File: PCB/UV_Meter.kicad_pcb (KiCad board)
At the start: 2 copper layers, 50.8 x 15.2 mm, 11 parts, among them SW1 SW_Push, U1 ATtiny85-20PU

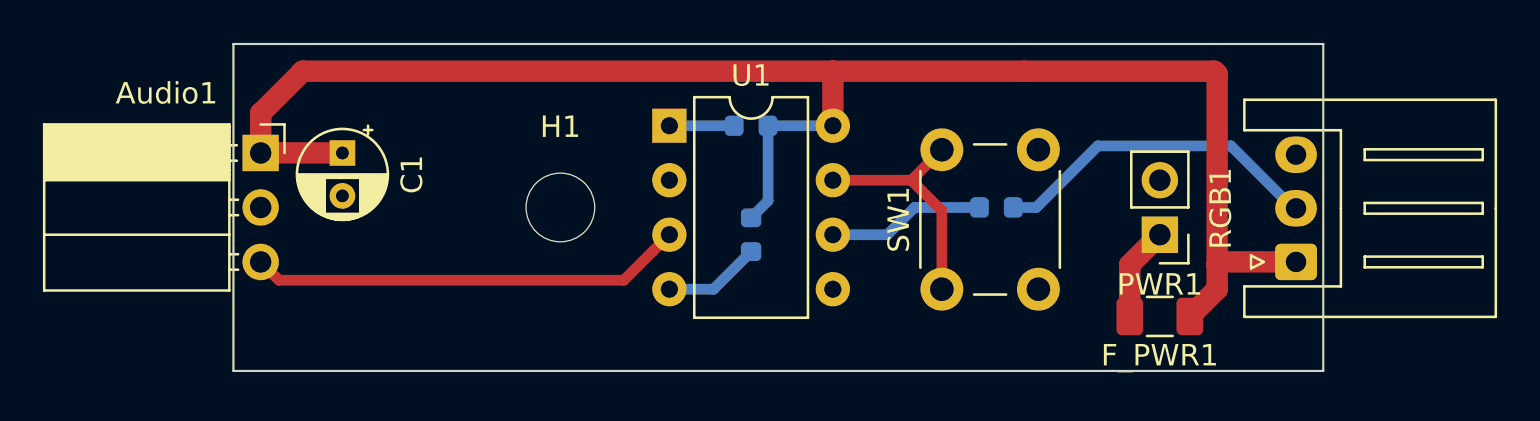
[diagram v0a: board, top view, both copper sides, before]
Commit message: improve label placement
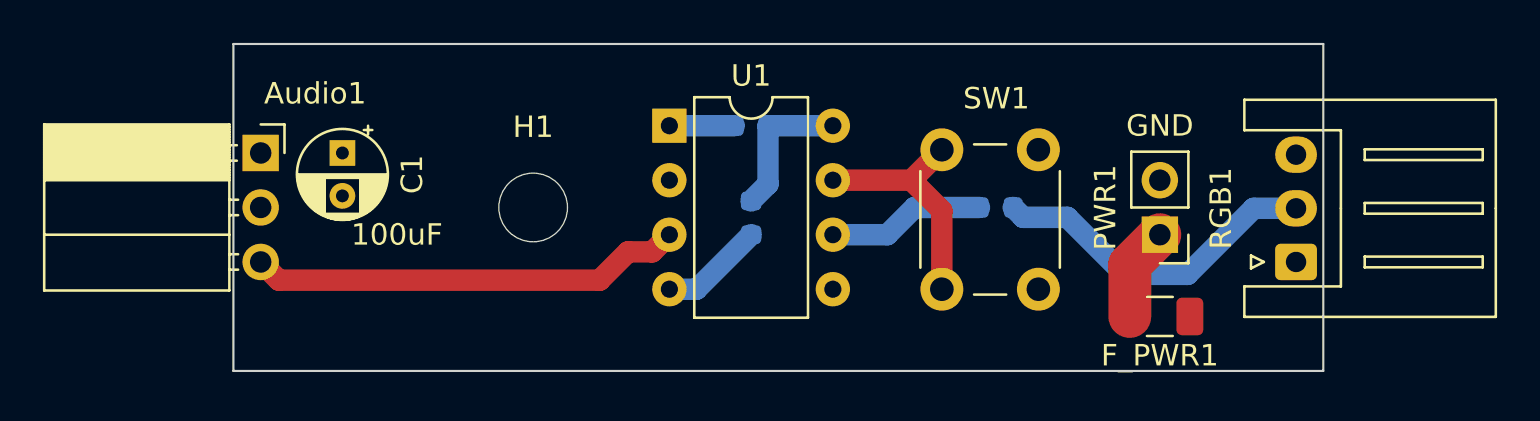
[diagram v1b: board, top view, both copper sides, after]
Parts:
- removed C2: 100nF, Capacitor_SMD:C_0603_1608Metric
- added C_uC1: 100nF, Capacitor_SMD:C_0603_1608Metric, B.Cu at (47.0, 32.2)
- moved H1 1.27 mm to (36.8, 31.8)
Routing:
- net +5V: track 76.4 -> 6.85 mm
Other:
- net class Default: trace_width 0.5 -> 1
- net class Power added: clearance 0.5, trace_width 2, via_dia 1, via_drill 0.4
- board text added: "GND"

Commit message: fix labels, move power labels
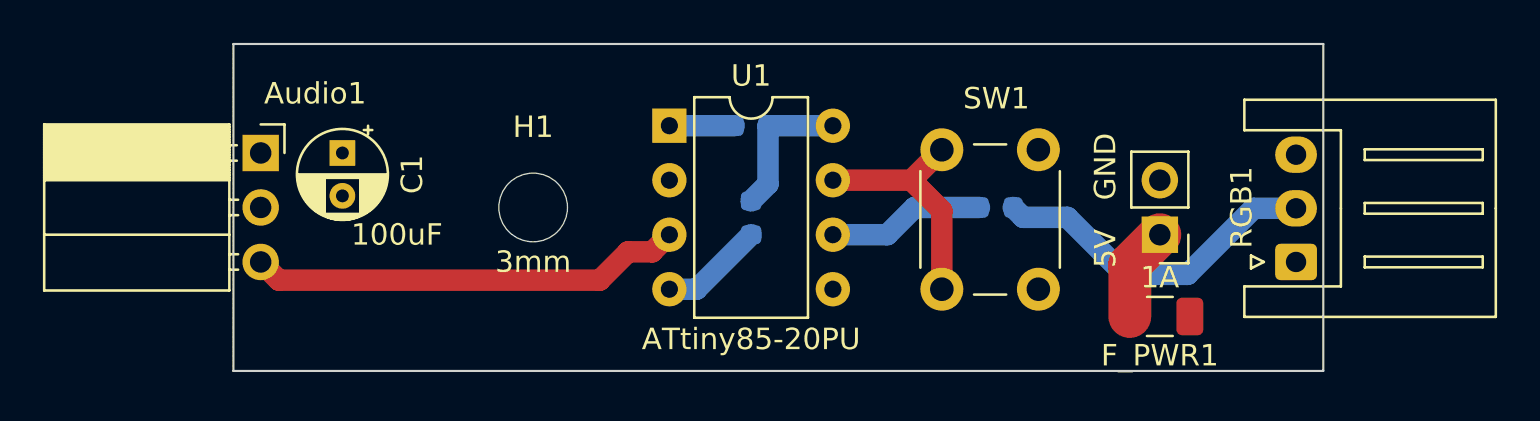
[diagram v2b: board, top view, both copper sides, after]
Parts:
- renumbered PWR1 to PWR
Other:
- board text added: "3mm"
- board text added: "5V"
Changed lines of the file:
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@@
   (general
     (thickness 1.6)
-    (drawings 4)
+    (drawings 6)
     (tracks 27)
     (zones 0)
@@
     (solder_mask_min_width 0.25)
     (aux_axis_origin 0 0)
-    (visible_elements FFFFFF7F)
+    (visible_elements 7FFFFFFF)
     (pcbplotparams
-      (layerselection 0x310fc_ffffffff)
+      (layerselection 0x010fc_ffffffff)
       (usegerberextensions false)
       (usegerberattributes false)
@@
     (descr "JST XH series connector, S3B-XH-A (http://www.jst-mfg.com/product/pdf/eng/eXH.pdf), generated with kicad-footprint-generator")
     (tags "connector JST XH horizontal")
-    (fp_text reference RGB1 (at 2.5 -3.5 90) (layer F.SilkS)
+    (fp_text reference RGB1 (at 2.54 -2.54 90) (layer F.SilkS)
       (effects (font (size 1 1) (thickness 0.15)))
     )
@@
       (effects (font (size 1 1) (thickness 0.15)))
     )
-    (fp_text value ATtiny85-20PU (at 3.81 9.95) (layer F.Fab)
+    (fp_text value ATtiny85-20PU (at 3.81 9.95) (layer F.SilkS)
       (effects (font (size 1 1) (thickness 0.15)))
     )
@@
     (descr "Through hole straight pin header, 1x02, 2.54mm pitch, single row")
     (tags "Through hole pin header THT 1x02 2.54mm single row")
-    (fp_text reference PWR1 (at 2.54 1.27 270) (layer F.SilkS)
+    (fp_text reference PWR (at 2.54 1.905 270) (layer F.Fab)
       (effects (font (size 1 1) (thickness 0.15)))
     )
@@
       (effects (font (size 1 1) (thickness 0.15)))
     )
-    (fp_text value 1A (at 0 1.82 180) (layer B.SilkS)
+    (fp_text value 1A (at 0 1.82 180) (layer F.SilkS)
       (effects (font (size 1 1) (thickness 0.15)))
     )
@@
     )
   )
-  (gr_text GND (at 66.04 27.94) (layer F.SilkS)
+  (gr_text 5V (at 63.5 33.655 90) (layer F.SilkS)
     (effects (font (size 1 1) (thickness 0.15)))
   )
+  (gr_text 3mm (at 36.83 34.29) (layer F.SilkS)
+    (effects (font (size 1 1) (thickness 0.15)))
+  )
+  (gr_text GND (at 63.5 29.845 90) (layer F.SilkS)
+    (effects (font (size 1 1) (thickness 0.15)))
+  )

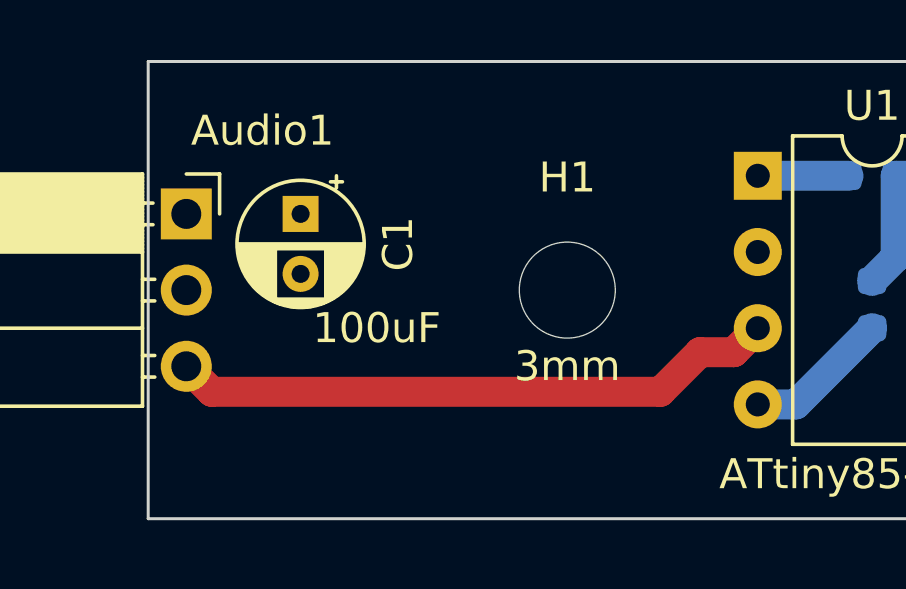
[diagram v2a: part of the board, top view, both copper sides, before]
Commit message: name Volumeter v2019/06, add logo
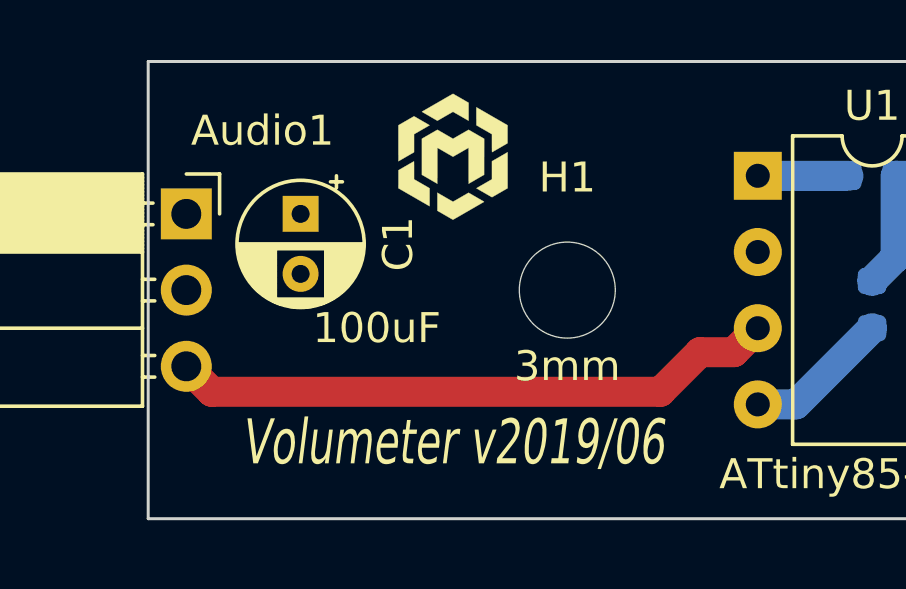
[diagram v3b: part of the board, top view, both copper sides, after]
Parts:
- added G***: LOGO, MF custom:mf_logo_5mm, F.Cu at (33.0, 27.3)
- renumbered PWR to PWR1
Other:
- board text added: "Volumeter v2019/06"
- board text added: "© Modisch Fabrications"
